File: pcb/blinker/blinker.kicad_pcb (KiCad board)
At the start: 2 copper layers, 96 x 86 mm, 14 parts, among them J1 Conn_01x04_Pin, J2 Conn_01x02_Pin_for_flashing, J3 Screw_Terminal_01x04, Q1 BC547, SW2 SW_MEC_5E, U1 ESP-12F

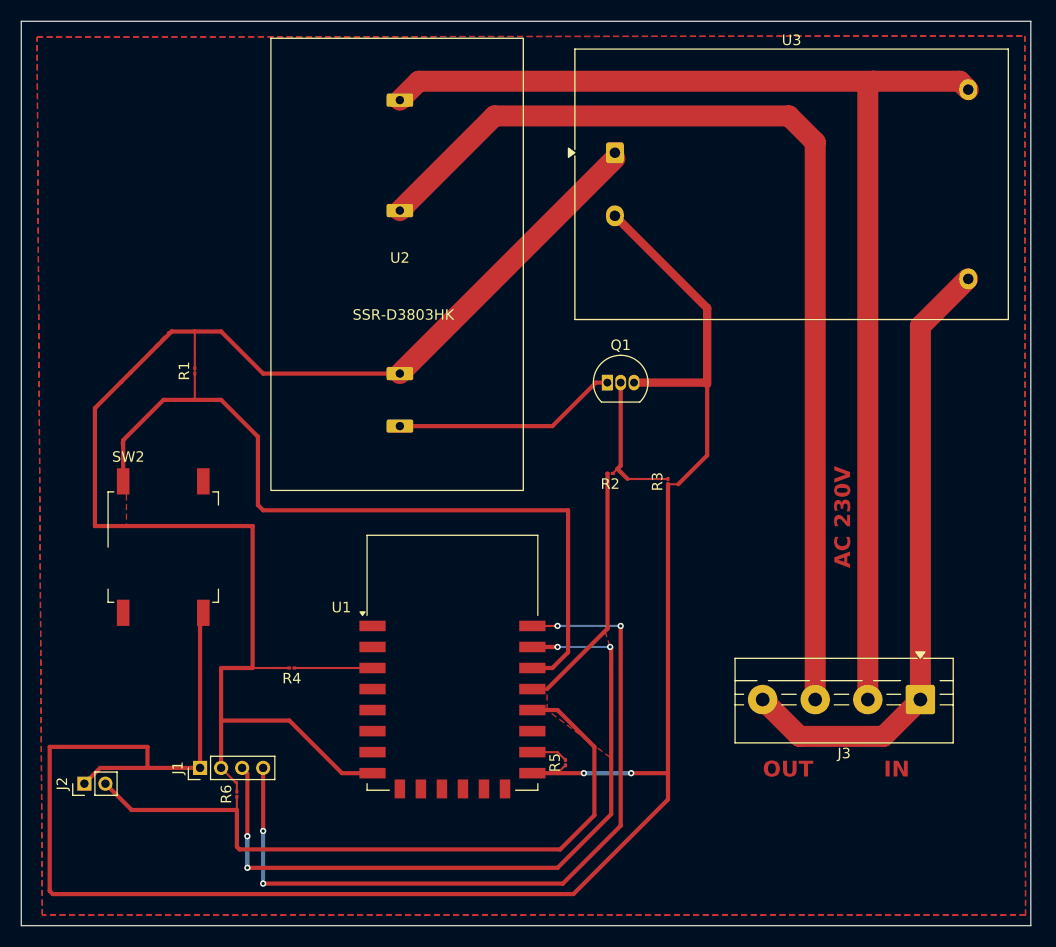
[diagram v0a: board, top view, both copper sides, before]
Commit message: Replace 0402 resistors with 2012 handSolder
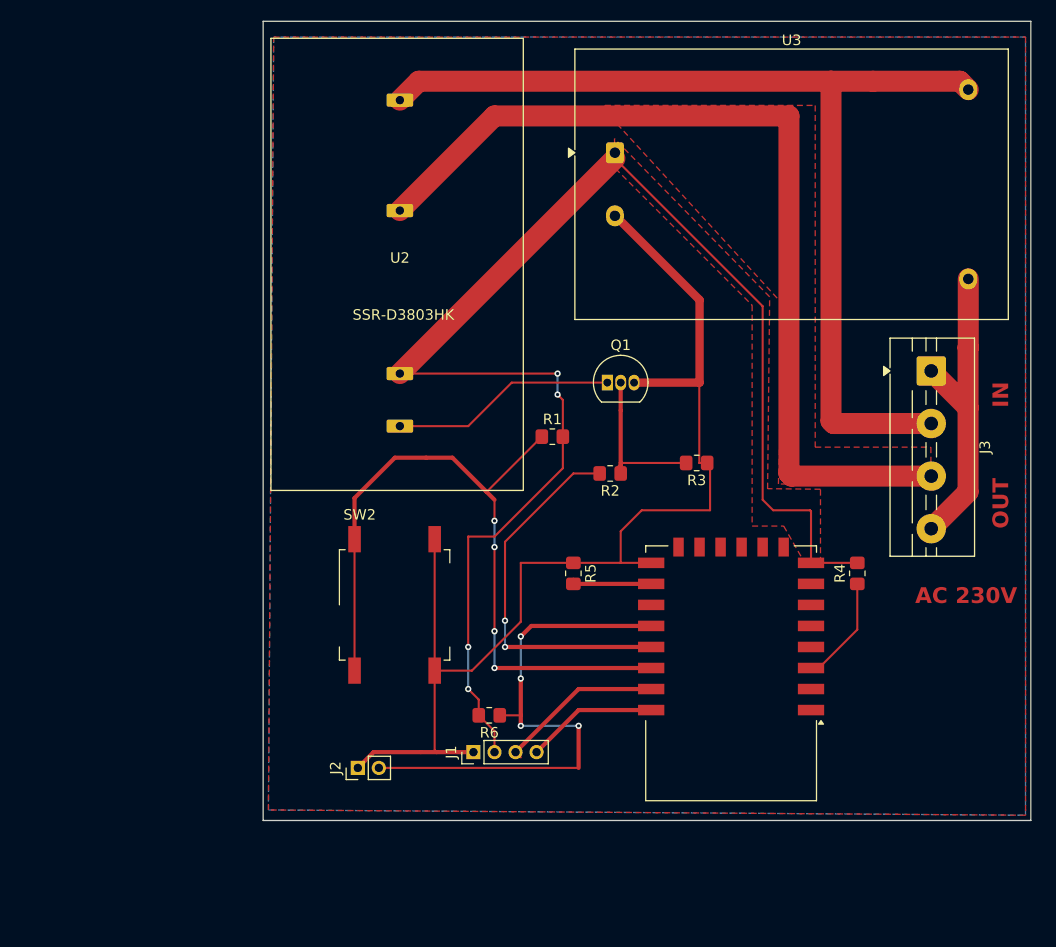
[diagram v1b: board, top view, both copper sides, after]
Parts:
- R1, R2, R3, R4, R5, R6: footprint Resistor_SMD:R_01005_0402Metric -> Resistor_SMD:R_0805_2012Metric_Pad1.20x1.40mm_HandSolder
- moved R4 54.5 mm to (137.0, 80.0), turned to 90 degrees
- moved R1 34.6 mm to (108.0, 67.0), turned to 0 degrees
- moved J3 31.3 mm to (144.0, 60.8), turned to -90 degrees
- moved U1 26.5 mm to (125.0, 89.5), turned to 180 degrees
- moved J1 26.0 mm to (100.5, 97.0)
- moved J2 26.0 mm to (89.5, 98.5)
- moved R6 25.1 mm to (102.0, 93.5), turned to 180 degrees
- moved SW2 22.7 mm to (93.0, 83.0)
- moved R5 18.0 mm to (110.0, 80.0), turned to -90 degrees
- moved R3 3.25 mm to (121.7, 69.5), turned to 180 degrees
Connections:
- SW2 pad 2: unconnected-(SW2-Pad2) -> Net-(U1-GPIO5)
- SW2 pad 3: unconnected-(SW2-K-Pad3) -> GND
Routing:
- net GND: track 196.4 -> 110.7 mm, vias 2 -> 0
- net Net-(J1-Pin_4): track 74.7 -> 12.6 mm, vias 4 -> 0
- net Net-(J1-Pin_3): track 69.9 -> 16.1 mm, vias 4 -> 0
- net Net-(J3-Pin_1): track 59.8 -> 30.2 mm
- net Net-(J2-Pin_2): track 69.4 -> 51.8 mm, vias 0 -> 4
- net Net-(J3-Pin_2): track 114.1 -> 97.1 mm
- net Net-(U1-GPIO4): track 24.3 -> 35.6 mm, vias 0 -> 2
- net Net-(J3-Pin_3): track 97.3 -> 88.4 mm
- net Net-(U1-GPIO5): track 76.0 -> 71.3 mm, vias 0 -> 4
- net Net-(U1-GPIO15): track 3.81 -> 7.61 mm
- net Net-(U1-EN): track 7.43 -> 10.3 mm
- net +3.3V: track 142.5 -> 140.2 mm, vias 0 -> 4
- added copper zone on B.Cu, net +3.3V
- added copper zone on F.Cu, net Net-(J3-Pin_3)
- removed copper zone on F.Cu, net Net-(U1-GPIO4)
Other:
- board size 96 x 86 mm -> 73 x 76 mm

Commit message: Update Relay pins
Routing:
- net Net-(J3-Pin_2): track 97.1 -> 101.9 mm
- net Net-(J3-Pin_3): track 88.4 -> 91.9 mm
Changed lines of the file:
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@@
 		(sheetname "/")
 		(sheetfile "blinker.kicad_sch")
-		(units
-			(unit
-				(name "A")
-				(pins "2" "1" "3")
-			)
-		)
 		(attr through_hole)
 		(duplicate_pad_numbers_are_jumpers no)
@@
 		(sheetname "/")
 		(sheetfile "blinker.kicad_sch")
-		(units
-			(unit
-				(name "A")
-				(pins "1" "2")
-			)
-		)
 		(attr smd)
 		(duplicate_pad_numbers_are_jumpers no)
@@
 		(sheetname "/")
 		(sheetfile "blinker.kicad_sch")
-		(units
-			(unit
-				(name "A")
-				(pins "1" "2" "3" "4")
-			)
-		)
 		(attr through_hole)
 		(duplicate_pad_numbers_are_jumpers no)
@@
 		(sheetname "/")
 		(sheetfile "blinker.kicad_sch")
-		(units
-			(unit
-				(name "A")
-				(pins "1" "2" "3" "4")
-			)
-		)
 		(attr through_hole)
 		(duplicate_pad_numbers_are_jumpers no)
@@
 		(sheetname "/")
 		(sheetfile "blinker.kicad_sch")
-		(units
-			(unit
-				(name "A")
-				(pins "1" "2")
-			)
-		)
 		(attr through_hole)
 		(duplicate_pad_numbers_are_jumpers no)
@@
 		(at 93.5 50.5)
 		(property "Reference" "U2"
-			(at 0 -0.5 0)
+			(at -5 -4.5 90)
 			(unlocked yes)
 			(layer "F.SilkS")
@@
 		(sheetname "/")
 		(sheetfile "blinker.kicad_sch")
-		(units
-			(unit
-				(name "A")
-				(pins "3" "4" "1" "2")
-			)
-		)
 		(attr smd)
 		(duplicate_pad_numbers_are_jumpers no)
@@
 		)
 		(fp_text user "SSR-D3803HK"
-			(at -4.5 5.5 0)
+			(at -4.5 9.5 90)
 			(unlocked yes)
 			(layer "F.SilkS")
@@
 		)
 		(pad "1" thru_hole roundrect
-			(at 0 -15.5)
+			(at 0 -11.5)
 			(size 2.54 1.27)
 			(drill 0.8)
@@
 		)
 		(pad "2" thru_hole roundrect
-			(at 0 -5)
+			(at 0 -1.5)
 			(size 2.54 1.27)
 			(drill 0.8)
@@
 		(sheetname "/")
 		(sheetfile "blinker.kicad_sch")
-		(units
-			(unit
-				(name "A")
-				(pins "1" "2")
-			)
-		)
 		(attr smd)
 		(duplicate_pad_numbers_are_jumpers no)
@@
 		(sheetname "/")
 		(sheetfile "blinker.kicad_sch")
-		(units
-			(unit
-				(name "A")
-				(pins "1" "3" "2" "9" "10" "11" "12" "13" "14" "8" "15" "18" "22" "17"
-					"21" "19" "20" "6" "7" "5" "16" "4"
-				)
-			)
-		)
 		(attr smd)
 		(duplicate_pad_numbers_are_jumpers no)
@@
 		(sheetname "/")
 		(sheetfile "blinker.kicad_sch")
-		(units
-			(unit
-				(name "A")
-				(pins "1" "2" "3" "4")
-			)
-		)
 		(attr through_hole)
 		(duplicate_pad_numbers_are_jumpers no)
@@
 		(sheetname "/")
 		(sheetfile "blinker.kicad_sch")
-		(units
-			(unit
-				(name "A")
-				(pins "1" "2")
-			)
-		)
 		(attr smd)
 		(duplicate_pad_numbers_are_jumpers no)
@@
 		(sheetname "/")
 		(sheetfile "blinker.kicad_sch")
-		(units
-			(unit
-				(name "A")
-				(pins "1" "2" "4" "3")
-			)
-		)
 		(attr smd)
 		(duplicate_pad_numbers_are_jumpers no)
@@
 		(sheetname "/")
 		(sheetfile "blinker.kicad_sch")
-		(units
-			(unit
-				(name "A")
-				(pins "1" "2")
-			)
-		)
 		(attr smd)
 		(duplicate_pad_numbers_are_jumpers no)
@@
 		(sheetname "/")
 		(sheetfile "blinker.kicad_sch")
-		(units
-			(unit
-				(name "A")
-				(pins "1" "2")
-			)
-		)
 		(attr smd)
 		(duplicate_pad_numbers_are_jumpers no)
@@
 		(sheetname "/")
 		(sheetfile "blinker.kicad_sch")
-		(units
-			(unit
-				(name "A")
-				(pins "1" "2")
-			)
-		)
 		(attr smd)
 		(duplicate_pad_numbers_are_jumpers no)
@@
 	)
 	(segment
-		(start 134.5 33.2)
-		(end 95.3 33.2)
+		(start 147.5525 34)
+		(end 146.7525 33.2)
 		(width 2)
 		(layer "F.Cu")
@@
 	)
 	(segment
-		(start 147.5525 34)
-		(end 146.7525 33.2)
+		(start 134.5 33.2)
+		(end 134.5 65.5)
 		(width 2)
 		(layer "F.Cu")
@@
 	(segment
 		(start 134.5 33.2)
-		(end 134.5 65.5)
+		(end 93.8 33.2)
+		(width 2)
+		(layer "F.Cu")
+		(net "Net-(J3-Pin_2)")
+	)
+	(segment
+		(start 93.8 33.2)
+		(end 93.5 33.5)
 		(width 2)
 		(layer "F.Cu")
@@
 	)
 	(segment
-		(start 95.3 33.2)
+		(start 93.5 33.5)
 		(end 93.5 35)
 		(width 2)
@@
 	)
 	(segment
+		(start 93.5 35)
+		(end 93.5 39)
+		(width 2)
+		(layer "F.Cu")
+		(net "Net-(J3-Pin_2)")
+	)
+	(segment
 		(start 147.5325 72.25)
 		(end 147.5325 64.25)
@@
 	)
 	(segment
-		(start 102.5 36.5)
-		(end 93.5 45.5)
+		(start 130.5 36.5)
+		(end 130.5 70.5)
+		(width 2)
+		(layer "F.Cu")
+		(net "Net-(J3-Pin_3)")
+	)
+	(segment
+		(start 130.5 70.5)
+		(end 130.75 70.75)
 		(width 2)
 		(layer "F.Cu")
@@
 	(segment
 		(start 130.5 36.5)
-		(end 130.5 70.5)
+		(end 102.5 36.5)
 		(width 2)
 		(layer "F.Cu")
@@
 	)
 	(segment
-		(start 130.5 70.5)
-		(end 130.75 70.75)
+		(start 93.5 45.5)
+		(end 93.5 49)
 		(width 2)
 		(layer "F.Cu")
@@
 	)
 	(segment
-		(start 130.5 36.5)
+		(start 93.5 45.5)
 		(end 102.5 36.5)
 		(width 2)
@@
 	)
 	(zone
-		(net "Net-(J3-Pin_3)")
+		(net "GND")
 		(layer "F.Cu")
 		(hatch edge 0.5)
-		(priority 1)
 		(connect_pads
 			(clearance 0.8)
@@
 		(polygon
 			(pts
-				(xy 113 35.5) (xy 133 35.5) (xy 133 68) (xy 144 68) (xy 144 71.5) (xy 129.5 71.5) (xy 130 54.5)
-				(xy 113 36)
+				(xy 81.831162 29.040677) (xy 152.511215 29.361494) (xy 152.13967 102.347029) (xy 81.5 102)
 			)
 		)
 	)
 	(zone
-		(net "+3.3V")
+		(net "Net-(J3-Pin_3)")
 		(layer "F.Cu")
 		(hatch edge 0.5)
-		(priority 2)
+		(priority 1)
 		(connect_pads
 			(clearance 0.8)
@@
 		(polygon
 			(pts
-				(xy 114 41.5) (xy 127 54.5) (xy 127 75.5) (xy 130 75.5) (xy 132 79) (xy 133.5 79) (xy 133.5 72)
-				(xy 128.47053 71.945889) (xy 128.666817 53.701483) (xy 113.910247 38.665683)
+				(xy 113 35.5) (xy 133 35.5) (xy 133 68) (xy 144 68) (xy 144 71.5) (xy 129.5 71.5) (xy 130 54.5)
+				(xy 113 36)
 			)
 		)
 	)
 	(zone
-		(net "GND")
+		(net "+3.3V")
 		(layer "F.Cu")
 		(hatch edge 0.5)
+		(priority 2)
 		(connect_pads
 			(clearance 0.8)
@@
 		(polygon
 			(pts
-				(xy 81.5 29) (xy 153 29) (xy 153 103) (xy 81 102.5)
+				(xy 114 41.5) (xy 127 54.5) (xy 127 75.5) (xy 130 75.5) (xy 132 79) (xy 133.5 79) (xy 133.5 72)
+				(xy 128.47053 71.945889) (xy 128.666817 53.701483) (xy 113.910247 38.665683)
 			)
 		)

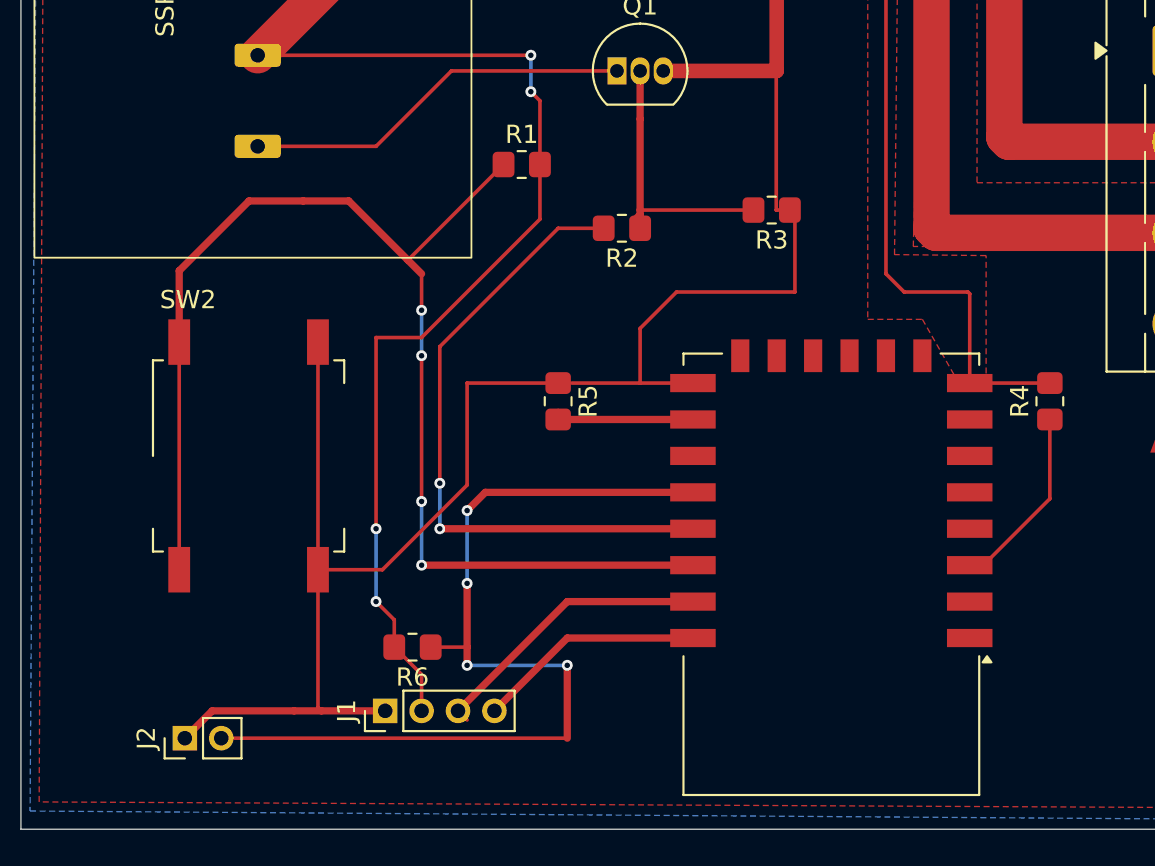
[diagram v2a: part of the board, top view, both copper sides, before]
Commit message: Change label pos on PCB
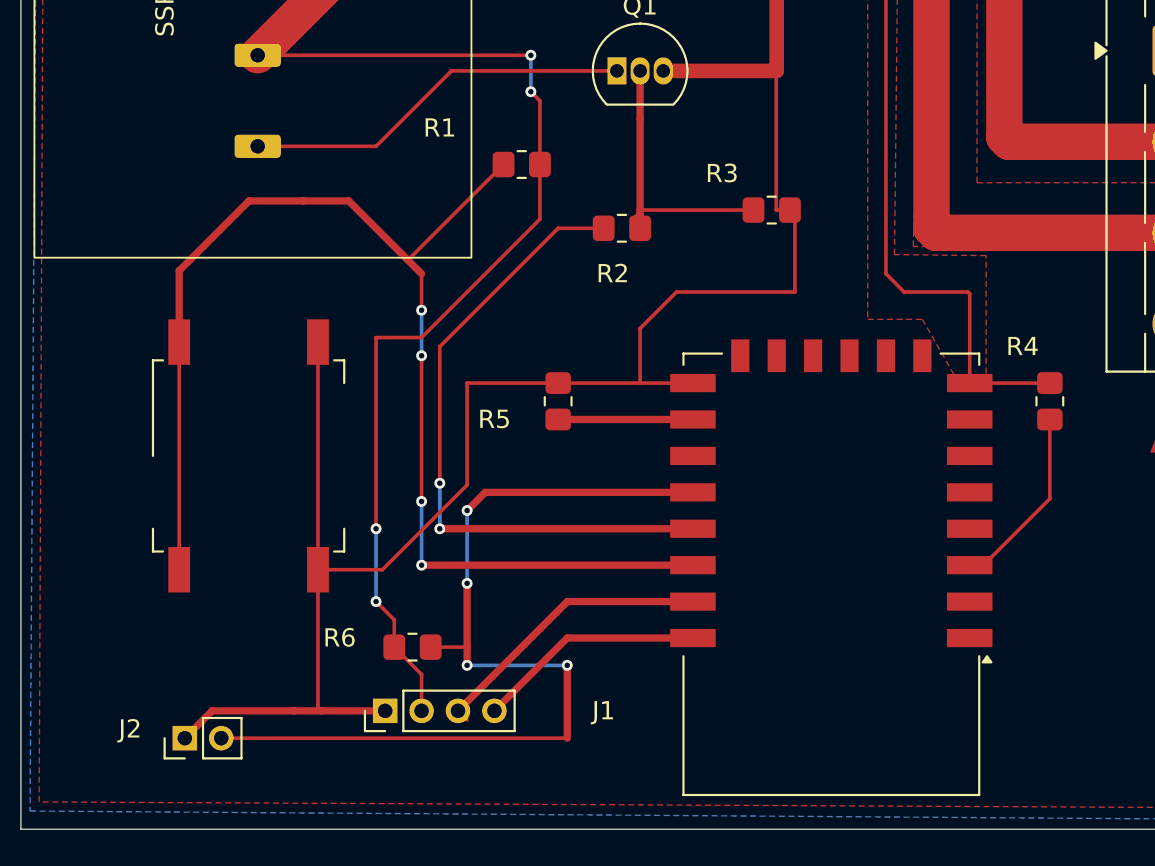
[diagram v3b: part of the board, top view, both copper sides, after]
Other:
- board text added: "Blinker"
- board text added: "TS"
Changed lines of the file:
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@@
 		)
 		(property "Value" "BC547"
-			(at 1.27 2.79 0)
+			(at 4.77 2.79 0)
 			(layer "F.Fab")
 			(effects
@@
 		(tags "resistor handsolder")
 		(property "Reference" "R5"
-			(at 0 -1.65 270)
+			(at 1 3.5 0)
 			(layer "F.SilkS")
 			(effects
@@
 		)
 		(property "Value" "10k"
-			(at 0 1.65 270)
+			(at 2.5 3 0)
 			(layer "F.Fab")
 			(effects
@@
 		(tags "Through hole pin header THT 1x04 2.00mm single row")
 		(property "Reference" "J1"
-			(at 0 -2.11 90)
+			(at 0 12 180)
 			(layer "F.SilkS")
 			(effects
@@
 		)
 		(property "Value" "Conn_01x04_Pin"
-			(at 0 8.11 90)
+			(at -3.5 9.5 180)
 			(layer "F.Fab")
 			(effects
@@
 		(tags "Through hole pin header THT 1x02 2.00mm single row")
 		(property "Reference" "J2"
-			(at 0 -2.11 90)
+			(at 0.5 -3 180)
 			(layer "F.SilkS")
 			(effects
@@
 		)
 		(property "Value" "Conn_01x02_Pin_for_flashing"
-			(at 0 4.11 90)
+			(at -2 3 180)
 			(layer "F.Fab")
 			(effects
@@
 		(tags "resistor handsolder")
 		(property "Reference" "R6"
-			(at 0 -1.65 0)
+			(at 4 0.5 0)
 			(layer "F.SilkS")
 			(effects
@@
 		)
 		(property "Value" "10k"
-			(at 0 1.65 0)
+			(at 3.5 -1 0)
 			(layer "F.Fab")
 			(effects
@@
 		)
 		(property "Value" "ESP-12F"
-			(at -0.06 -12.78 0)
+			(at -11.5 -5.5 90)
 			(layer "F.Fab")
 			(effects
@@
 		)
 		(property "Value" "Screw_Terminal_01x04"
-			(at 7.25 4.92 90)
+			(at -6.25 6.0325 90)
 			(layer "F.Fab")
 			(effects
@@
 		(tags "resistor handsolder")
 		(property "Reference" "R4"
-			(at 0 -1.65 90)
+			(at 3 -1.5 180)
 			(layer "F.SilkS")
 			(effects
@@
 		)
 		(property "Value" "10k"
-			(at 0 1.65 90)
+			(at 3 1 180)
 			(layer "F.Fab")
 			(effects
@@
 		(tags "switch normally-open pushbutton push-button")
 		(property "Reference" "SW2"
-			(at -3.325 -8.575 180)
+			(at 0.5 3 180)
 			(layer "F.SilkS")
+			(hide yes)
 			(effects
 				(font
@@
 		)
 		(property "Value" "SW_MEC_5E"
-			(at 0.475 8.825 180)
+			(at -4.5 11 180)
 			(layer "F.Fab")
 			(effects
@@
 		)
 		(fp_text user "${REFERENCE}"
-			(at -2.31 -1.75 0)
+			(at 0.5 -3.5 0)
 			(layer "F.Fab")
 			(effects
@@
 		(tags "resistor handsolder")
 		(property "Reference" "R2"
-			(at 0 -1.65 180)
+			(at 0.5 -2.5 180)
 			(layer "F.SilkS")
 			(effects
@@
 		)
 		(property "Value" "1k"
-			(at 0 1.65 180)
+			(at -1.5 -2.5 180)
 			(layer "F.Fab")
 			(effects
@@
 		(tags "resistor handsolder")
 		(property "Reference" "R3"
-			(at 0 -1.65 180)
+			(at 2.725 2 180)
 			(layer "F.SilkS")
 			(effects
@@
 		)
 		(property "Value" "10k"
-			(at 0 1.65 180)
+			(at 0.225 2 180)
 			(layer "F.Fab")
 			(effects
@@
 		(tags "resistor handsolder")
 		(property "Reference" "R1"
-			(at 0 -1.65 0)
+			(at -4.5 -2 0)
 			(layer "F.SilkS")
 			(effects
@@
 		)
 		(property "Value" "10k"
-			(at 0 1.65 0)
+			(at -1.5 -2 0)
 			(layer "F.Fab")
 			(effects
@@
 			)
 			(justify left bottom)
+		)
+	)
+	(gr_text "Blinker"
+		(at 142.5 88 0)
+		(layer "F.Mask")
+		(effects
+			(font
+				(size 1 1)
+				(thickness 0.15)
+			)
+			(justify left bottom)
+		)
+	)
+	(gr_text "TS"
+		(at 149.5 101 0)
+		(layer "F.Mask")
+		(effects
+			(font
+				(size 1 1)
+				(thickness 0.15)
+			)
+			(justify left bottom)

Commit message: Update Relay footprint
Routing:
- net Net-(J3-Pin_2): track 101.9 -> 99.4 mm
- net Net-(J3-Pin_3): track 91.9 -> 92.9 mm
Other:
- board size 73 x 76 mm -> 68 x 76 mm
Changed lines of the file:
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@@
 		(tags "Through hole pin header THT 1x04 2.00mm single row")
 		(property "Reference" "J1"
-			(at 0 12 180)
+			(at -2.5 -1.5 180)
 			(layer "F.SilkS")
 			(effects
@@
 		(tags "Through hole pin header THT 1x02 2.00mm single row")
 		(property "Reference" "J2"
-			(at 0.5 -3 180)
+			(at 2.5 0.5 180)
 			(layer "F.SilkS")
 			(effects
@@
 		)
 		(property "Value" "Conn_01x02_Pin_for_flashing"
-			(at -2 3 180)
+			(at -4 8.5 180)
 			(layer "F.Fab")
 			(effects
@@
 		(duplicate_pad_numbers_are_jumpers no)
 		(fp_rect
-			(start -12.261011 -21.384347)
-			(end 11.738989 21.615653)
+			(start -6 -21.384347)
+			(end 6 21.615653)
 			(stroke
 				(width 0.1)
@@
 		)
 		(pad "1" thru_hole roundrect
-			(at 0 -11.5)
+			(at 0 -14)
 			(size 2.54 1.27)
 			(drill 0.8)
@@
 		)
 		(pad "2" thru_hole roundrect
-			(at 0 -1.5)
+			(at 0 -4)
 			(size 2.54 1.27)
 			(drill 0.8)
@@
 		)
 		(property "Value" "SW_MEC_5E"
-			(at -4.5 11 180)
+			(at 1 -9 180)
 			(layer "F.Fab")
 			(effects
@@
 	)
 	(gr_rect
-		(start 80.5 27.499999)
+		(start 85.5 27.499999)
 		(end 153.5 103.5)
 		(stroke
@@
 	)
 	(segment
-		(start 93.8 33.2)
-		(end 93.5 33.5)
-		(width 2)
-		(layer "F.Cu")
-		(net "Net-(J3-Pin_2)")
-	)
-	(segment
 		(start 138.5 33.2)
 		(end 134.5 33.2)
@@
 	(segment
 		(start 93.5 33.5)
-		(end 93.5 35)
+		(end 93.5 36.5)
 		(width 2)
 		(layer "F.Cu")
@@
 	)
 	(segment
-		(start 93.5 35)
-		(end 93.5 39)
+		(start 93.8 33.2)
+		(end 93.5 33.5)
 		(width 2)
 		(layer "F.Cu")
@@
 	)
 	(segment
-		(start 130.5 36.5)
-		(end 130.5 70.5)
+		(start 144.0325 70.75)
+		(end 130.75 70.75)
 		(width 2)
 		(layer "F.Cu")
@@
 	(segment
 		(start 130.5 70.5)
-		(end 130.75 70.75)
+		(end 130.5 36.5)
 		(width 2)
 		(layer "F.Cu")
@@
 	(segment
 		(start 130.5 36.5)
-		(end 102.5 36.5)
+		(end 105 36.5)
 		(width 2)
 		(layer "F.Cu")
@@
 	)
 	(segment
-		(start 93.5 45.5)
-		(end 93.5 49)
+		(start 102 46.5)
+		(end 93.5 46.5)
 		(width 2)
 		(layer "F.Cu")
@@
 	)
 	(segment
-		(start 93.5 45.5)
-		(end 102.5 36.5)
+		(start 130.75 70.75)
+		(end 130.5 70.5)
 		(width 2)
 		(layer "F.Cu")
@@
 	)
 	(segment
-		(start 130.75 70.75)
-		(end 144.0325 70.75)
+		(start 105 43.5)
+		(end 102 46.5)
+		(width 2)
+		(layer "F.Cu")
+		(net "Net-(J3-Pin_3)")
+	)
+	(segment
+		(start 105 36.5)
+		(end 105 43.5)
 		(width 2)
 		(layer "F.Cu")
@@
 		(polygon
 			(pts
-				(xy 81.831162 29.040677) (xy 152.511215 29.361494) (xy 152.13967 102.347029) (xy 81.5 102)
+				(xy 86.66539 29.06262) (xy 152.511215 29.361494) (xy 152.13967 102.347029) (xy 86.33422 102.023749)
 			)
 		)
@@
 		(polygon
 			(pts
-				(xy 81.5 29) (xy 81 102.5) (xy 153 103) (xy 153 29)
+				(xy 86.751701 29) (xy 86.251453 102.536468) (xy 153 103) (xy 153 29)
 			)
 		)
